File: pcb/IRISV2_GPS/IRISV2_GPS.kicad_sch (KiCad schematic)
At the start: 27 parts, among them J1 Conn_01x06_MountingPin, U1 NEO-M9N, U2 lna

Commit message: lr2021 reroute, maybe need to do stuff with gps lna bc iip3 and ip1db
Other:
- note added: "current lna won't work because it would destroy the signal from out of band interferece, too low p1db and iip3"
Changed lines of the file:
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@@
+		)
+	)
+	(text "current lna won't work because it would destroy the signal from out of band interferece, too low p1db and iip3"
+		(exclude_from_sim no)
+		(at 211.582 137.414 0)
+		(effects
+			(font
+				(size 1.27 1.27)
+			)
 		)
 	)

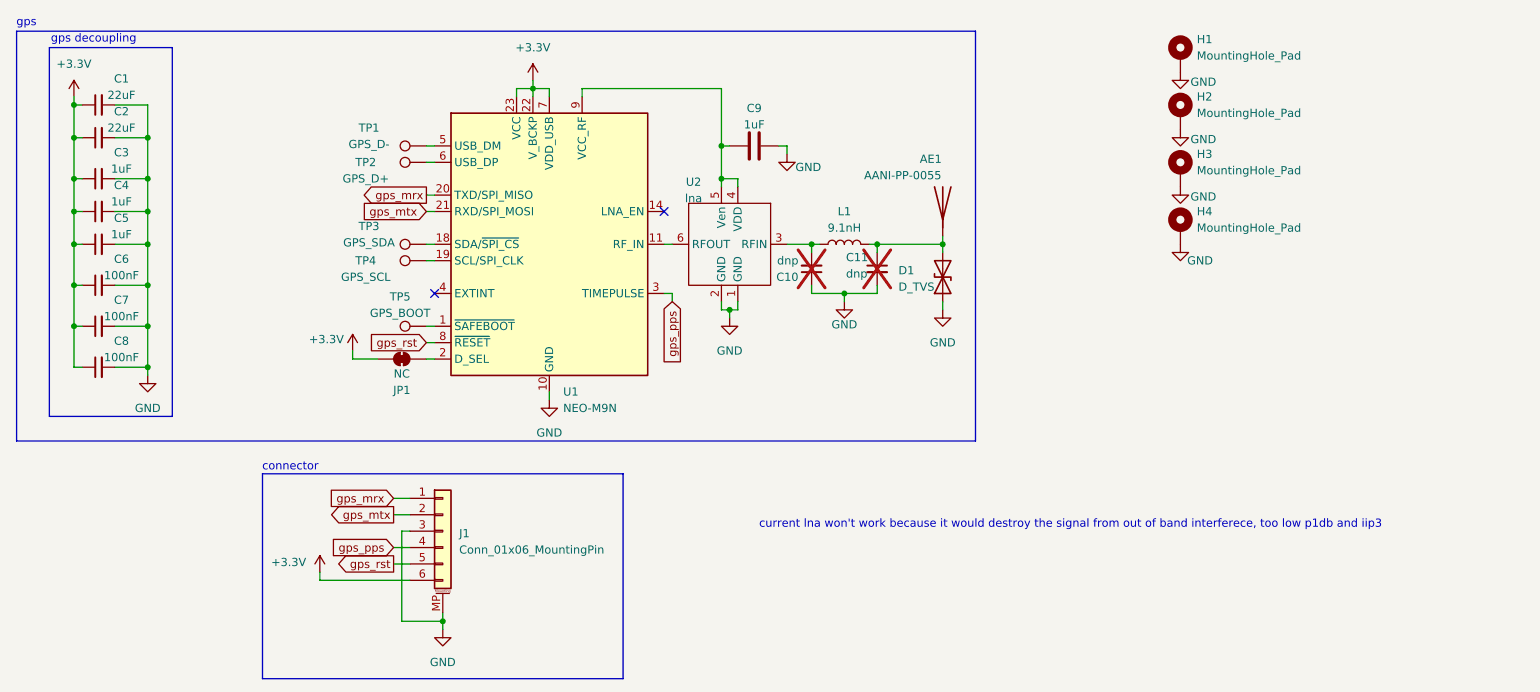
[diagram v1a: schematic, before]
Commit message: fixed some issues, lr2021 matching is now 0201 - todo change trace width to match pad width like ref design, see todo for rest
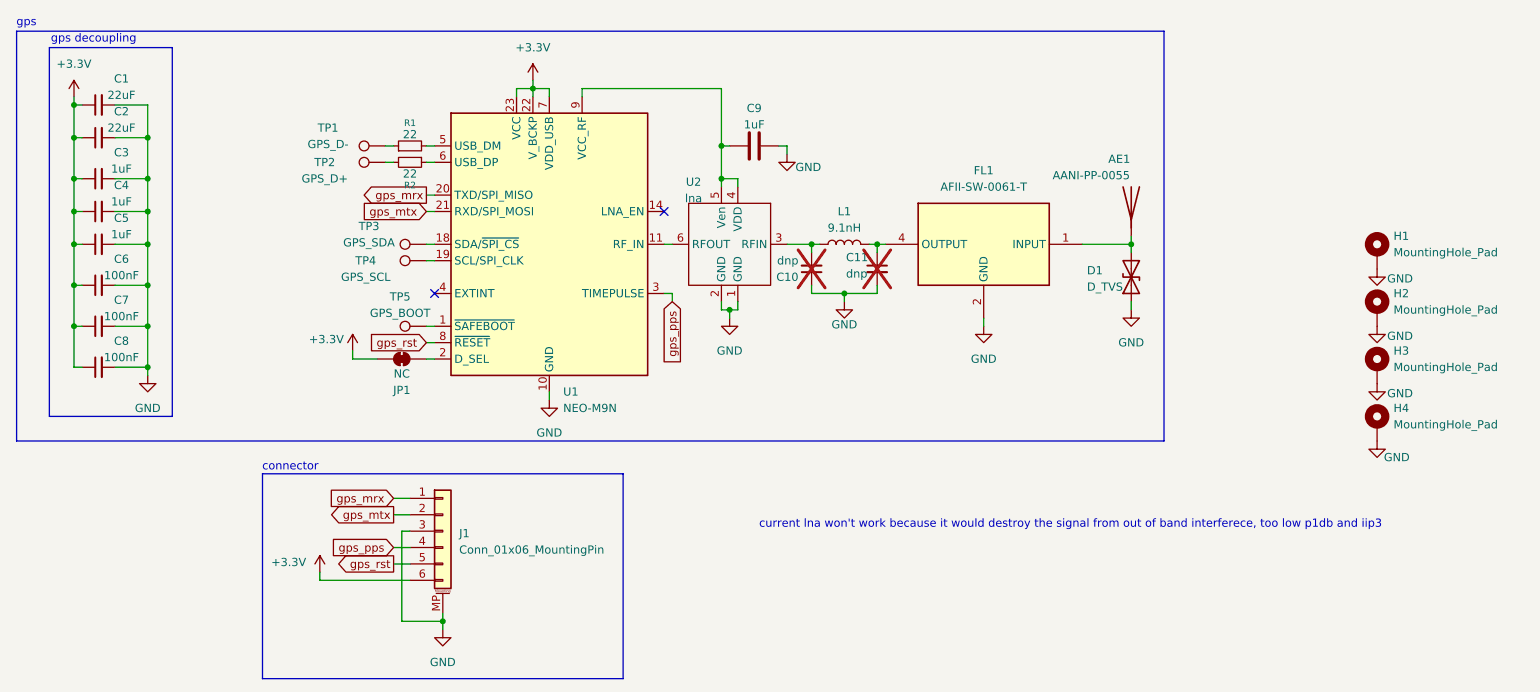
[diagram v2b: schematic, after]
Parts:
- added FL1: AFII-SW-0061-T, AFII-SW-0061-T:AFIISW0061T, symbol AFII-SW-0061-T:AFII-SW-0061-T
- added R1, R2: 22, Resistor_SMD:R_0402_1005Metric, symbol Device:R_Small
- C10, C11: footprint Capacitor_SMD:C_0402_1005Metric -> Capacitor_SMD:C_0201_0603Metric
- L1: footprint Inductor_SMD:L_0402_1005Metric -> Inductor_SMD:L_0201_0603Metric
- TP1, TP2, TP3, TP4, TP5: footprint TestPoint:TestPoint_Pad_D2.0mm -> TestPoint:TestPoint_Pad_D1.5mm
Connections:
- net GND: now also FL1.2 (GND)
- net at AE1.1 (A), D1.2 (A2): now also FL1.1 (INPUT); no longer C11.1, L1.2
- net at TP1.1: now also R1.1; no longer U1.5 (USB_DM)
- net at U1.6 (USB_DP): now also R2.1; no longer TP2.1
- new net: C11.1, FL1.4 (OUTPUT), L1.2
- new net: R2.2, TP2.1
- new net: R1.2, U1.5 (USB_DM)
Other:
- moved on the sheet: AE1, D1, H1, H2, H3, H4, TP1, TP2
